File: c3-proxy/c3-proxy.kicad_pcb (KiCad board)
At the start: 4 copper layers, 74.8 x 50 mm, 76 parts, among them J1 J-SAMTEC-TFM-120-X1-XXX-D-RA, J2 SFM-120-02-X-DH, J3 USB_C_Receptacle_USB2.0_16P, J4 Barrel_Jack, J5 Conn_01x04, Q1 DMP2035UQ-7, Q2 DMP2035UQ-7, Q3 DMP2035UQ-7, Q4 DMP2035UQ-7, Q6 31-DMN2053UQ-13CT-ND, SW1 C&K PCM13SMTR, U1 MCP2221AxST, U2 INA226, U3 LTC4412xS6, U4 LTC4412xS6, U5 TS5A21366, U6 MAX892LEUA+T, U7 MIC23050-SYML, U8 LTC4412xS6, U9 IP4234CZ6,125

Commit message: did like... everything...
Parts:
- removed TP18, TP19, TP20, TP21, TP22, TP23: Test-Point, oresat-misc:TestPoint-0.75mm-th
- added D6: 1N4001, Diode_THT:D_DO-35_SOD27_P7.62mm_Horizontal, F.Cu at (134.4, 137.2)
- added SW2: SW_DP3T, oresat-misc:CL-SB-23B-XX, F.Cu at (153.6, 120.9)
- C1: value 4.7uF -> 1uF
- C3, C4: footprint oresat-passives:0603-A -> oresat-passives:0805-A
- C6: value 4.7uF -> 100n
- D3: value GREEN -> AMB
- HW1, HW2, HW3: value M1.6_Mounting_Hole -> M3 mounting hole; footprint oresat-misc:M1.6 Mounting Hole -> MountingHole:MountingHole_3.2mm_M3
- J4: footprint Connector_BarrelJack:BarrelJack_CUI_PJ-102AH_Horizontal -> Connector_BarrelJack:BarrelJack_GCT_DCJ200-10-A_Horizontal
- R16, R17, R18, R20, R21, R22, R23: value 0 -> 100
- moved FID1 66.1 mm to (105.2, 133.1)
- moved FID2 65.5 mm to (170.7, 133.1)
- moved J5 1.62 mm to (111.5, 131.6)
- moved J4 1.11 mm to (150.6, 129.0)
- moved FID3 0.72 mm to (170.7, 91.9)
- turned D2 to 90 degrees
- turned D3 to 90 degrees
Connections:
- R13 pad 1: Net-(D2-K) -> Net-(D2-A)
- R13 pad 2: GND -> 3.3V
- R14 pad 1: Net-(D3-K) -> Net-(D3-A)
- R14 pad 2: GND -> 3.3V
- U1 pad 2: Net-(D3-A) -> Net-(D3-K)
- U1 pad 3: Net-(D2-A) -> Net-(D2-K)
- U1 pad 5: /C3-UART-RX -> /opd/MCP_URx
- U1 pad 6: /C3-UART-TX -> /opd/MCP_UTx
- U3 pad 3: Net-(U3-CTL) -> unconnected-(U3-CTL-Pad3)
- U3 pad 4: Net-(U3-STAT) -> unconnected-(U3-STAT-Pad4)
- U4 pad 3: Net-(U4-CTL) -> unconnected-(U4-CTL-Pad3)
- U4 pad 4: Net-(U4-STAT) -> unconnected-(U4-STAT-Pad4)
- U8 pad 3: Net-(U8-CTL) -> unconnected-(U8-CTL-Pad3)
- U8 pad 4: Net-(U8-STAT) -> unconnected-(U8-STAT-Pad4)
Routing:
- net /C3-UART-TX: track 78.4 -> 105.0 mm, vias 4 -> 6
- net /opd/MCP_UTx: track 0.00 -> 26.0 mm, vias 0 -> 2
- net /opd/MCP_URx: track 0.00 -> 23.8 mm, vias 0 -> 2
- net /C3-UART-RX: track 71.4 -> 89.5 mm, vias 2 -> 4
- net Net-(D3-K): track 2.26 -> 13.5 mm
- net Net-(D3-A): track 12.8 -> 2.26 mm
- net Net-(U4-CTL): track 6.53 -> 0.00 mm
- net Net-(U4-STAT): track 5.96 -> 0.00 mm, vias 1 -> 0
- net Net-(U3-CTL): track 5.93 -> 0.00 mm
- net Net-(D2-K): track 2.26 -> 7.69 mm
- net Net-(U3-STAT): track 5.40 -> 0.00 mm, vias 1 -> 0
- net Net-(D2-A): track 7.19 -> 2.26 mm
- net 3.3V: track 35.3 -> 40.2 mm
- net VUSB: track 48.7 -> 52.8 mm, vias 11 -> 10
- net Net-(U8-STAT): track 2.55 -> 0.00 mm
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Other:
- board text added: "0) c3 mode 1) disconnected 2) card mode"
- board text added: "OreSat ${PROJECTNAME}"
- board text removed: "FlatSat ${PROJECTNAME}"

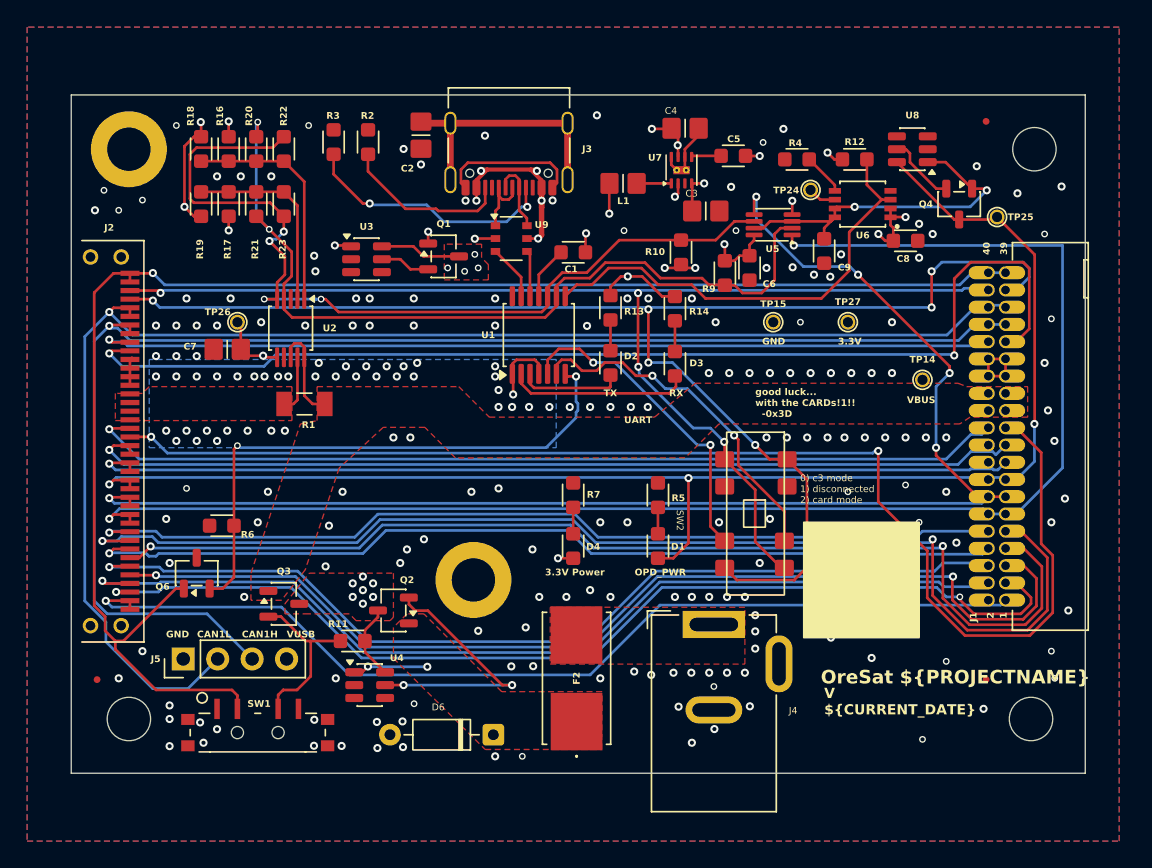
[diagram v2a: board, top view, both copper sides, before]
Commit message: v1.0 of the C3 Proxy sent off to fabrication.
Added makefile and README. Fixed a bunch of BOM issues, mostly just EOL and out of stock components. Fixed wrong footprints in the BOM, and switched diode from TH to SMT. Cleaned up some traces for funsies,
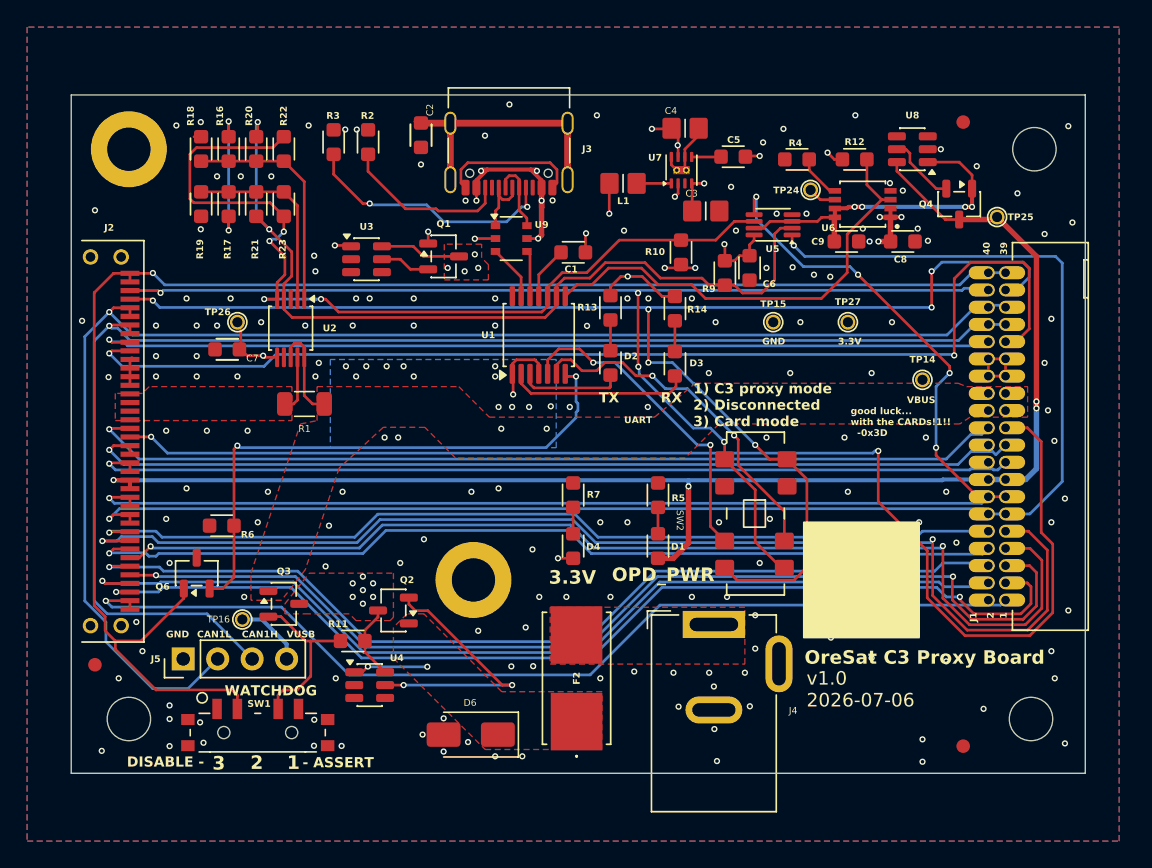
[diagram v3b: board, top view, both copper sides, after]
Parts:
- added TP16: Test-Point, oresat-misc:TestPoint-0.75mm-th, F.Cu at (115.9, 128.7)
- C1, C8, C9: value 1uF -> 1u
- C2, C7: value 100nF -> 100n; footprint oresat-passives:0805-A -> oresat-passives:0603-A
- C3, C4: value 4.7uF -> 4.7u
- C5: value 470pF -> 470p
- D1, D4: value GREEN -> GRN
- D6: value 1N4001 -> SS5150; footprint Diode_THT:D_DO-35_SOD27_P7.62mm_Horizontal -> Diode_SMD:D_SMA
- FID1, FID2, FID3: footprint Fiducial:Fiducial_0.5mm_Mask1mm -> Fiducial:Fiducial_1mm_Mask2mm
- J1: value J-SAMTEC-TFM-120-X1-XXX-D-RA -> TFM-120-X1-XXX-D-RA
- J2: value SFM-120-02-X-DH -> SFM-120-02-L-DH
- J4: value Barrel_Jack -> DCJ200-10-A-K1-K
- R1: footprint oresat-passives:1206-B -> Resistor_SMD:R_1206_3216Metric
- R19: value 0 -> 100
- moved FID2 5.19 mm to (169.0, 138.0)
- moved C9 1.79 mm to (160.4, 100.8), turned to 0 degrees
- moved FID3 1.69 mm to (169.0, 92.0)
- moved D6 1.67 mm to (132.7, 137.2)
- moved FID1 1.11 mm to (105.0, 132.0)
- moved C8 0.21 mm to (164.6, 100.8)
- moved C5 0.06 mm to (152.1, 94.5)
- turned R13 to -90 degrees
- turned R14 to -90 degrees
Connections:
- J2 pad MP: (no net) -> GND
- J4 pad 3: (no net) -> GND
- J5 pad 4: VUSB -> Net-(J5-Pin_4)
- R13 pad 1: Net-(D2-A) -> 3.3V
- R13 pad 2: 3.3V -> Net-(D2-A)
- R14 pad 1: Net-(D3-A) -> 3.3V
- R14 pad 2: 3.3V -> Net-(D3-A)
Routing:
- net VUSB: track 52.8 -> 20.8 mm
- net GND: track 35.1 -> 26.0 mm, vias 206 -> 173
- net 3.3V: track 40.2 -> 48.3 mm, vias 31 -> 28
- net Net-(J5-Pin_4): track 0.00 -> 5.11 mm
- net Net-(Q4-D): track 25.8 -> 26.0 mm, vias 2 -> 4
- net /OPD_PWR: track 107.2 -> 107.4 mm, vias 3 -> 4
- added copper zone on In2.Cu, net GND
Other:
- board text added: "${TITLE}"
- board text added: "- ASSERT"
- board text added: "1"
- board text added: "1) C3 proxy mode 2) Disconnected 3) Card mode"
- board text added: "2"
- board text added: "3"
- board text added: "DISABLE -"
- board text added: "WATCHDOG"
- board text added: "v${REVISION} ${ISSUE_DATE}"
- board text removed: "0) c3 mode 1) disconnected 2) card mode"
- board text removed: "3.3V Power"
- board text removed: "OreSat ${PROJECTNAME}"
- board text removed: "V${REVISION} ${CURRENT_DATE}"

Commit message: decreased size to fit in EU, transistor orientation
changed DC jack to be edge connected.
adjusted layout in top-right corner to still fit mounting hole.
fixed transistor orientation by switching to GSD symbols
moved SW2 and clarified silkscreen with boxes
changed via sizes to be standardized
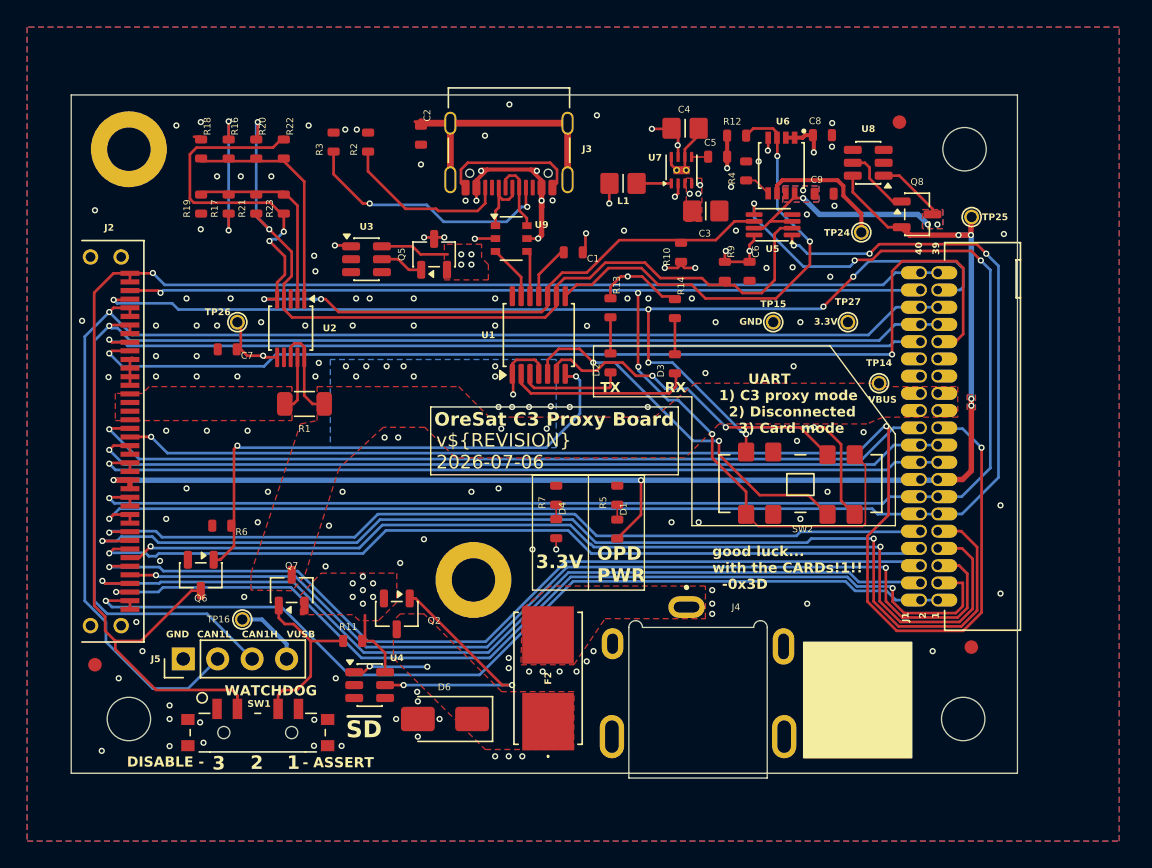
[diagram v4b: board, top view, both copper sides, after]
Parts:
- removed Q1, Q3, Q4: DMP2035UQ-7, Package_TO_SOT_SMD:SOT-23-3
- added Q5: DMP2035UQ-7, Package_TO_SOT_SMD:SOT-23-3, F.Cu at (130.0, 101.8)
- added Q7: DMP2035UQ-7, Package_TO_SOT_SMD:SOT-23-3, F.Cu at (119.5, 126.5)
- added Q8: DMP2035UQ-7, Package_TO_SOT_SMD:SOT-23-3, F.Cu at (165.6, 98.8)
- C1, C2, C5, C6, C7, C8, C9, D1, D2, D3, D4, R10, R11, R12, R16, R17, R18, R19, R2, R20, R21, R22, R23, R3, R4, R5, R6, R7, R9: footprint oresat-passives:0603-A -> oresat-passives:0603-C-NOSILK
- J4: value DCJ200-10-A-K1-K -> Barrel_Jack_Switch_MountingPin; footprint Connector_BarrelJack:BarrelJack_GCT_DCJ200-10-A_Horizontal -> oresat-connectors:SAMESKY_PJ-069B-SMT-TR
- R13, R14: value 10k -> 4.7k; footprint oresat-passives:0603-A -> oresat-passives:0603-C-NOSILK
- moved C8 9.83 mm to (158.6, 93.0)
- moved R12 8.87 mm to (152.3, 93.0)
- moved J4 8.51 mm to (148.6, 137.3)
- moved FID2 7.32 mm to (169.6, 130.7)
- moved U6 6.63 mm to (155.6, 95.2), turned to -90 degrees
- moved HW3 5.15 mm to (169.1, 94.0)
- moved HW1 5.00 mm to (169.0, 136.0)
- moved J1 5.00 mm to (166.5, 115.2)
- moved TP24 4.88 mm to (161.5, 100.1)
- moved FID3 4.70 mm to (164.3, 92.0)
- moved SW2 4.00 mm to (157.0, 118.7), turned to 0 degrees
- moved C9 3.89 mm to (158.8, 97.3)
- moved R4 3.85 mm to (153.0, 95.6), turned to 90 degrees
- moved U8 3.40 mm to (162.0, 95.0)
- moved D1 3.25 mm to (143.5, 122.0)
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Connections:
- Q2 pad 1: Net-(D6-K) -> Net-(Q2-G)
- Q2 pad 2: Net-(Q2-G) -> Net-(Q2-S)
- Q2 pad 3: Net-(Q1-S) -> Net-(D6-K)
- Q6 pad 1: /~{SD} -> /Power/USBShutdown
- Q6 pad 2: /Power/USBShutdown -> GND
- Q6 pad 3: GND -> /~{SD}
- R11 pad 2: Net-(Q1-S) -> Net-(Q2-S)
- U3 pad 6: Net-(Q1-S) -> Net-(Q2-S)
- U4 pad 6: Net-(Q1-S) -> Net-(Q2-S)
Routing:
- net Net-(Q1-S): track 12.1 -> 0.00 mm, vias 11 -> 0
- net Net-(Q2-S): track 0.00 -> 10.8 mm, vias 0 -> 11
- net /OPD_SDA: track 111.3 -> 102.1 mm, vias 2 -> 4
- net Net-(U6-~{FAULT}): track 2.09 -> 9.76 mm
- net /C3-UART-TX: track 105.0 -> 97.6 mm, vias 6 -> 7
- net 3.3V: track 48.3 -> 42.1 mm
- net /OPD_PWR: track 107.4 -> 102.2 mm, vias 4 -> 6
- net /CAN2_L: track 69.6 -> 64.4 mm
- net /SPARE9: track 87.5 -> 82.3 mm
- net /CAN1_L: track 106.3 -> 101.2 mm
- net /SPARE10: track 68.2 -> 63.1 mm
- net /CAN2_H: track 68.7 -> 63.7 mm
- net /SPARE8: track 68.3 -> 63.2 mm
- net /SPARE32: track 66.7 -> 61.7 mm
- net /SPARE22: track 68.2 -> 63.2 mm
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- added copper zone on B.Cu, net /OPD_PWR
- added copper zone on F.Cu, net /OPD_PWR
- added copper zone on F.Cu, net 3.3V
- added copper zone on F.Cu, net Net-(Q2-S)
- added copper zone on In2.Cu, net Net-(Q2-S)
- added copper zone on B.Cu, net Net-(Q8-D)
- added copper zone on F.Cu, net Net-(Q8-D)
- removed copper zone on F.Cu, net Net-(Q1-S)
- removed copper zone on In2.Cu, net Net-(Q1-S)
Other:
- board size 74.8 x 50 mm -> 69.8 x 50 mm
- board text added: "OPD PWR"
- board text added: "UART 1) C3 proxy mode 2) Disconnected 3) Card mode"
- board text added: "~{SD}"
- board text removed: "1) C3 proxy mode 2) Disconnected 3) Card mode"
- board text removed: "OPD_PWR"
- board text removed: "UART"
